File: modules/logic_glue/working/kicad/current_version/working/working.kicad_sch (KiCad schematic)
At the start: 0 parts

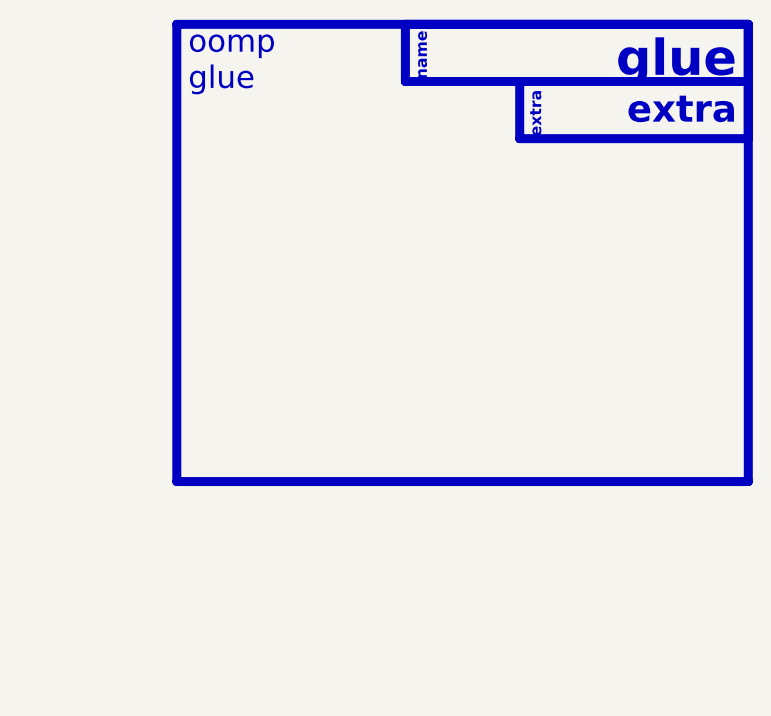
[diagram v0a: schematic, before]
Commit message: fixed formatting to be more consistent
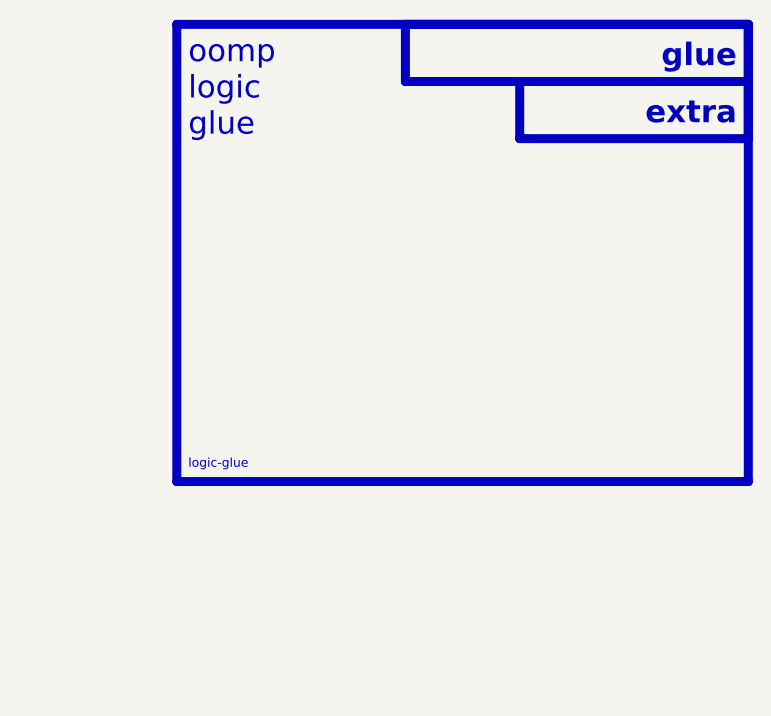
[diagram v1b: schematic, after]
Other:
- note added: "logic-glue"
- note added: "oomp logic glue"
- note removed: "name"
- note removed: "oomp glue"
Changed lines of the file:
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@@
   (rectangle (start 119.38 17.78) (end 157.48 24.13)
     (stroke (width 1) (type default))
-    (fill (type color) (color 0 0 0 0))
+    (fill (type none))
   )
   (rectangle (start 132.08 24.13) (end 157.48 30.48)
@@
     (fill (type none))
   )
-  (text "glue" (at 156.21 24.13 0)
-    (effects (font (size 4 4) (thickness 0.8) bold (color 255 255 255 1)) (justify right bottom))
-  )
-  (text "name" (at 121.92 24.13 90)
-    (effects (font (size 1.27 1.27) (thickness 0.254) bold (color 255 255 255 1)) (justify left bottom))
+  (text "glue" (at 156.21 22.86 0)
+    (effects (font (size 2.5 2.5) (thickness 0.8) bold) (justify right bottom))
   )
   (text "extra" (at 156.21 29.21 0)
-    (effects (font (size 3 3) (thickness 0.8) bold) (justify right bottom))
+    (effects (font (size 2.5 2.5) (thickness 0.8) bold) (justify right bottom))
   )
-  (text "oomp\nglue" (at 95.25 25.4 0)
+  (text "oomp\nlogic\nglue" (at 95.25 30.48 0)
     (effects (font (size 2.5 2.5)) (justify left bottom))
   )
-  (text "extra" (at 134.62 30.48 90)
-    (effects (font (size 1.27 1.27) (thickness 0.254) bold) (justify left bottom))
+  (text "logic-glue" (at 95.25 67.31 0)
+    (effects (font (size 1 1)) (justify left bottom))
   )
   (sheet_instances

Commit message: schematic formatting
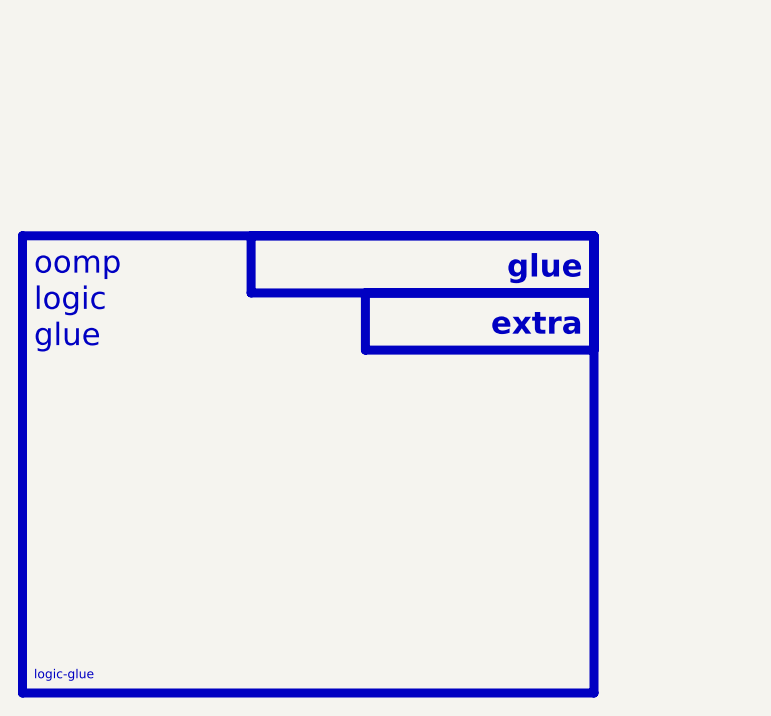
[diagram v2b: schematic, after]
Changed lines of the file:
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@@
 (kicad_sch (version 20230121) (generator eeschema)
-  (paper "A4")
-  (rectangle (start 93.98 17.78) (end 157.48 68.58)
+  (paper "A5")
+  (rectangle (start 76.835 41.275) (end 140.335 92.075)
     (stroke (width 1) (type default))
     (fill (type none))
   )
-  (rectangle (start 138.43 181.61) (end 138.43 181.61)
+  (rectangle (start 121.285 205.105) (end 121.285 205.105)
     (stroke (width 0) (type default))
     (fill (type none))
   )
-  (rectangle (start 119.38 17.78) (end 157.48 24.13)
+  (rectangle (start 102.235 41.275) (end 140.335 47.625)
     (stroke (width 1) (type default))
     (fill (type none))
   )
-  (rectangle (start 132.08 24.13) (end 157.48 30.48)
+  (rectangle (start 114.935 47.625) (end 140.335 53.975)
     (stroke (width 1) (type default))
     (fill (type none))
   )
-  (text "glue" (at 156.21 22.86 0)
+  (text "glue" (at 139.065 46.355 0)
     (effects (font (size 2.5 2.5) (thickness 0.8) bold) (justify right bottom))
   )
-  (text "extra" (at 156.21 29.21 0)
+  (text "extra" (at 139.065 52.705 0)
     (effects (font (size 2.5 2.5) (thickness 0.8) bold) (justify right bottom))
   )
-  (text "oomp\nlogic\nglue" (at 95.25 30.48 0)
+  (text "oomp\nlogic\nglue" (at 78.105 53.975 0)
     (effects (font (size 2.5 2.5)) (justify left bottom))
   )
-  (text "logic-glue" (at 95.25 67.31 0)
+  (text "logic-glue" (at 78.105 90.805 0)
     (effects (font (size 1 1)) (justify left bottom))
   )

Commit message: some works
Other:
- note added: "logic_glue"
- note removed: "logic-glue"
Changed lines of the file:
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@@
     (effects (font (size 2.5 2.5)) (justify left bottom))
   )
-  (text "logic-glue" (at 78.105 90.805 0)
+  (text "logic_glue" (at 78.105 90.805 0)
     (effects (font (size 1 1)) (justify left bottom))
   )
